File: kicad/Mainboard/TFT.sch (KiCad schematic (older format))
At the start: 2 parts, among them J7 Conn_01x10, Q2 BSS138

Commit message: - Added footprint library - TR-9 - Imported a few footprints - Designed a MicroSD card slot footprint - Assignment footprints to corresponding elements on schematic
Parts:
- J7: footprint (none) -> Connector_FFC-FPC:Hirose_FH12-10S-0.5SH_1x10-1MP_P0.50mm_Horizontal
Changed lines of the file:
@@
 EESchema Schematic File Version 4
-LIBS:Mainboard-cache
 EELAYER 30 0
 EELAYER END
@@
 F 0 "J7" H 6168 3125 50  0000 C CNN
 F 1 "Conn_01x10" H 6168 3216 50  0000 C CNN
-F 2 "" H 6250 3850 50  0001 C CNN
+F 2 "Connector_FFC-FPC:Hirose_FH12-10S-0.5SH_1x10-1MP_P0.50mm_Horizontal" H 6250 3850 50  0001 C CNN
 F 3 "~" H 6250 3850 50  0001 C CNN
 	1    6250 3850

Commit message: Added HMC RF switch Corrected SOIC footprints assignment
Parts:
- Q2: footprint TO_SOT_Packages_SMD:SOT-23 -> Package_TO_SOT_SMD:SOT-23
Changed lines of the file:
@@
 F 0 "Q2" H 4506 3796 50  0000 L CNN
 F 1 "BSS138" H 4506 3705 50  0000 L CNN
-F 2 "TO_SOT_Packages_SMD:SOT-23" H 4500 3675 50  0001 L CIN
+F 2 "Package_TO_SOT_SMD:SOT-23" H 4500 3675 50  0001 L CIN
 F 3 "https://www.fairchildsemi.com/datasheets/BS/BSS138.pdf" H 4300 3750 50  0001 L CNN
 	1    4300 3750

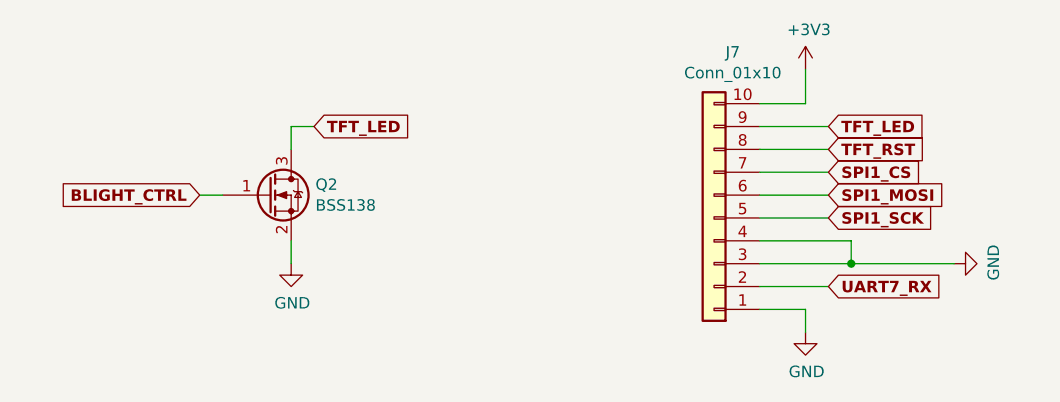
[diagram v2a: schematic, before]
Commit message: Added thermal vias to BGA6589 footprint Corrected USART to UART
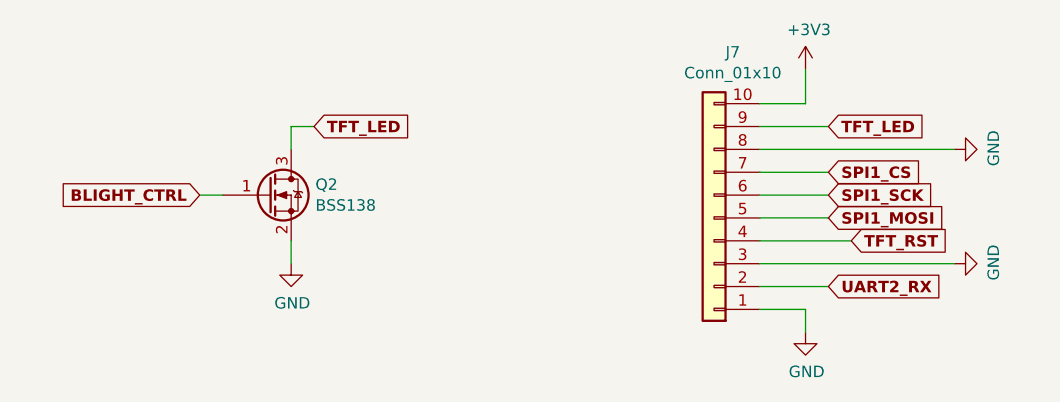
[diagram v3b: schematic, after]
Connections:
- net GND: now also J7.8 (Pin_8); no longer J7.4 (Pin_4)
- net SPI1_MOSI: now also J7.5 (Pin_5); no longer J7.6 (Pin_6)
- net SPI1_SCK: now also J7.6 (Pin_6); no longer J7.5 (Pin_5)
- net TFT_RST: now also J7.4 (Pin_4); no longer J7.8 (Pin_8)
- net UART7_RX renamed UART2_RX
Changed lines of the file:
@@
 Text GLabel 6750 3450 2    50   Input ~ 10
 TFT_LED
-Text GLabel 6750 3550 2    50   Input ~ 10
+Text GLabel 6850 3950 2    50   Input ~ 10
 TFT_RST
 Text GLabel 6750 3650 2    50   Input ~ 10
 SPI1_CS
+Text GLabel 6750 3850 2    50   Input ~ 10
+SPI1_MOSI
 Text GLabel 6750 3750 2    50   Input ~ 10
-SPI1_MOSI
-Text GLabel 6750 3850 2    50   Input ~ 10
 SPI1_SCK
 Wire Wire Line
 	6450 3450 6750 3450
-Wire Wire Line
-	6450 3550 6750 3550
 Wire Wire Line
 	6450 3650 6750 3650
@@
 	6450 4150 6750 4150
 Text GLabel 6750 4150 2    50   Input ~ 10
-UART7_RX
+UART2_RX
 $Comp
 L power:GND #PWR054
@@
 $EndComp
 Wire Wire Line
-	6450 4050 6850 4050
-Wire Wire Line
 	6450 3950 6850 3950
-Wire Wire Line
-	6850 3950 6850 4050
-Connection ~ 6850 4050
-Wire Wire Line
-	6850 4050 7300 4050
 $Comp
 L Mainboard-rescue:Conn_01x10-Connector_Generic J7
@@
 	-1   0    0    1
 $EndComp
+Wire Wire Line
+	6450 4050 7300 4050
+$Comp
+L power:GND #PWR0179
+U 1 1 5E47DF4D
+P 7300 3550
+F 0 "#PWR0179" H 7300 3300 50  0001 C CNN
+F 1 "GND" H 7305 3377 50  0000 C CNN
+F 2 "" H 7300 3550 50  0001 C CNN
+F 3 "" H 7300 3550 50  0001 C CNN
+	1    7300 3550
+	0    -1   -1   0
+$EndComp
+Wire Wire Line
+	6450 3550 7300 3550
 $EndSCHEMATC

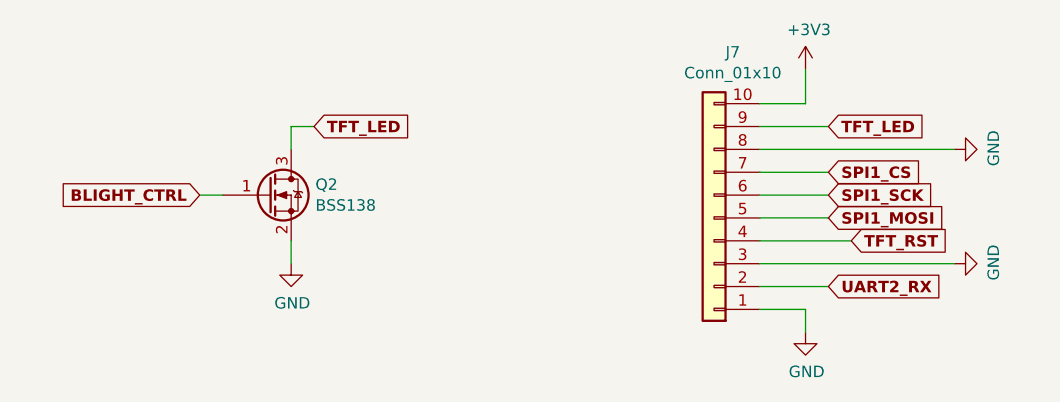
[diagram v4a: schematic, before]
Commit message: PCB - connected microSD card to STM32 & USB frontend path routed added a schottky diode PMEG4005ET.215 footprint changed connector J7 pinout - TFT_RST swapped with UART2_RX! schootky diode added to in series to mini USB connector PDF generated
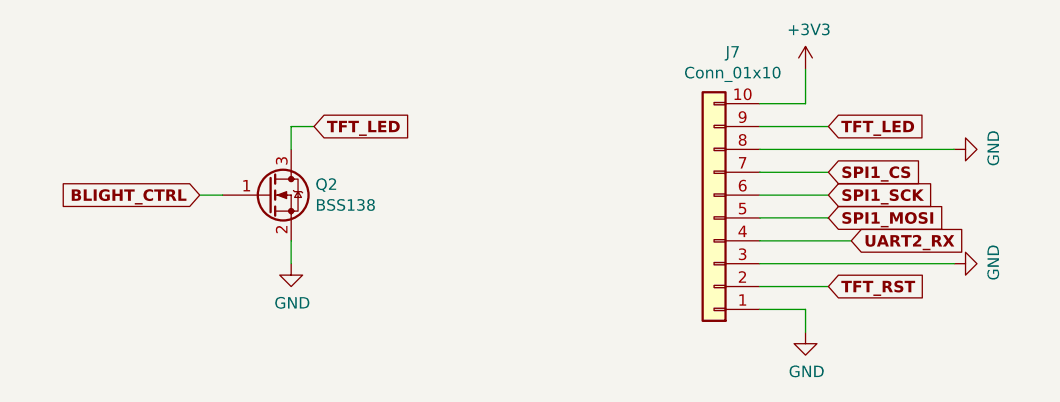
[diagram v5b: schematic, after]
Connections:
- net TFT_RST: now also J7.2 (Pin_2); no longer J7.4 (Pin_4)
- net UART2_RX: now also J7.4 (Pin_4); no longer J7.2 (Pin_2)
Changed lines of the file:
@@
 Text GLabel 6750 3450 2    50   Input ~ 10
 TFT_LED
-Text GLabel 6850 3950 2    50   Input ~ 10
+Text GLabel 6750 4150 2    50   Input ~ 10
 TFT_RST
 Text GLabel 6750 3650 2    50   Input ~ 10
@@
 Wire Wire Line
 	6450 4150 6750 4150
-Text GLabel 6750 4150 2    50   Input ~ 10
+Text GLabel 6850 3950 2    50   Input ~ 10
 UART2_RX
 $Comp

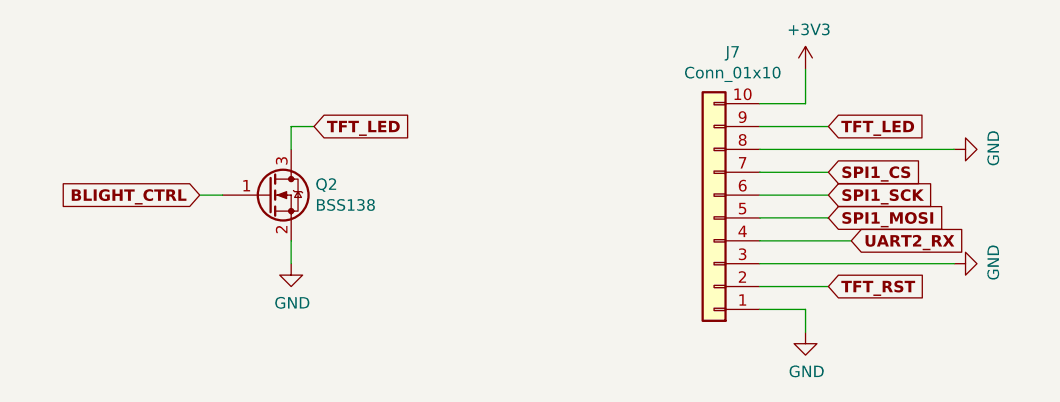
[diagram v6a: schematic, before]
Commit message: Critical J7 header pinout change! New schematic PCB plot
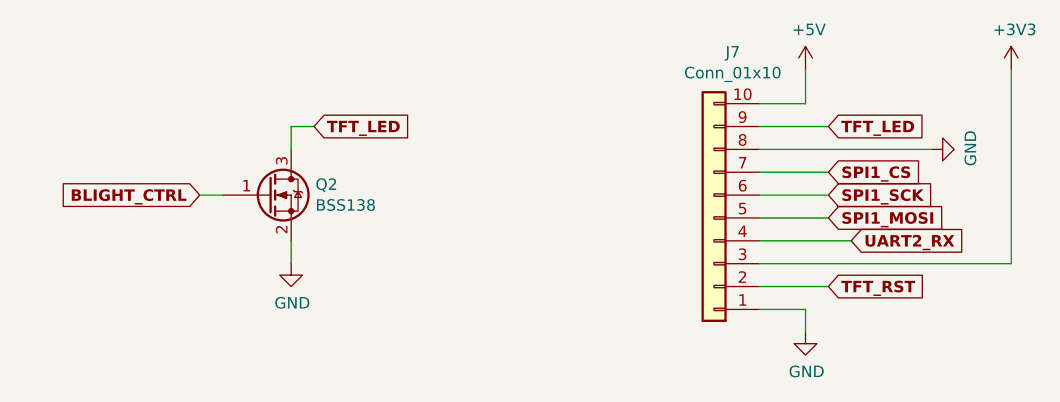
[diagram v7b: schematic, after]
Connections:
- net +3V3: now also J7.3 (Pin_3); no longer J7.10 (Pin_10)
- net GND: no longer J7.3 (Pin_3)
- new net +5V: J7.10 (Pin_10)
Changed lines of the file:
@@
 Wire Wire Line
 	6650 3350 6650 3200
-$Comp
-L power:+3V3 #PWR052
-U 1 1 5DF0DB74
-P 6650 3200
-F 0 "#PWR052" H 6650 3050 50  0001 C CNN
-F 1 "+3V3" H 6665 3373 50  0000 C CNN
-F 2 "" H 6650 3200 50  0001 C CNN
-F 3 "" H 6650 3200 50  0001 C CNN
-	1    6650 3200
-	1    0    0    -1
-$EndComp
 Wire Wire Line
 	6450 4250 6650 4250
@@
 Text GLabel 6850 3950 2    50   Input ~ 10
 UART2_RX
-$Comp
-L power:GND #PWR054
-U 1 1 5E1E62B4
-P 7300 4050
-F 0 "#PWR054" H 7300 3800 50  0001 C CNN
-F 1 "GND" H 7305 3877 50  0000 C CNN
-F 2 "" H 7300 4050 50  0001 C CNN
-F 3 "" H 7300 4050 50  0001 C CNN
-	1    7300 4050
-	0    -1   -1   0
-$EndComp
 Wire Wire Line
 	6450 3950 6850 3950
@@
 	-1   0    0    1
 $EndComp
+$Comp
+L power:+5V #PWR?
+U 1 1 5E4D13A0
+P 6650 3200
+AR Path="/5DEDCA32/5E4D13A0" Ref="#PWR?"  Part="1"
+AR Path="/5DF0AC25/5E4D13A0" Ref="#PWR0179"  Part="1"
+F 0 "#PWR0179" H 6650 3050 50  0001 C CNN
+F 1 "+5V" H 6665 3373 50  0000 C CNN
+F 2 "" H 6650 3200 50  0001 C CNN
+F 3 "" H 6650 3200 50  0001 C CNN
+	1    6650 3200
+	1    0    0    -1
+$EndComp
+$Comp
+L power:+3V3 #PWR?
+U 1 1 5E4D63A8
+P 7550 3200
+AR Path="/5DEDCA32/5E4D63A8" Ref="#PWR?"  Part="1"
+AR Path="/5DF0AC25/5E4D63A8" Ref="#PWR0194"  Part="1"
+F 0 "#PWR0194" H 7550 3050 50  0001 C CNN
+F 1 "+3V3" H 7565 3373 50  0000 C CNN
+F 2 "" H 7550 3200 50  0001 C CNN
+F 3 "" H 7550 3200 50  0001 C CNN
+	1    7550 3200
+	1    0    0    -1
+$EndComp
 Wire Wire Line
-	6450 4050 7300 4050
+	6450 3550 7200 3550
 $Comp
-L power:GND #PWR0179
-U 1 1 5E47DF4D
-P 7300 3550
-F 0 "#PWR0179" H 7300 3300 50  0001 C CNN
-F 1 "GND" H 7305 3377 50  0000 C CNN
-F 2 "" H 7300 3550 50  0001 C CNN
-F 3 "" H 7300 3550 50  0001 C CNN
-	1    7300 3550
+L power:GND #PWR0195
+U 1 1 5E4D8D3B
+P 7200 3550
+F 0 "#PWR0195" H 7200 3300 50  0001 C CNN
+F 1 "GND" H 7205 3377 50  0000 C CNN
+F 2 "" H 7200 3550 50  0001 C CNN
+F 3 "" H 7200 3550 50  0001 C CNN
+	1    7200 3550
 	0    -1   -1   0
 $EndComp
 Wire Wire Line
-	6450 3550 7300 3550
+	7550 3200 7550 4050
+Wire Wire Line
+	6450 4050 7550 4050
 $EndSCHEMATC

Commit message: added some decoupling caps, pull ups/downs
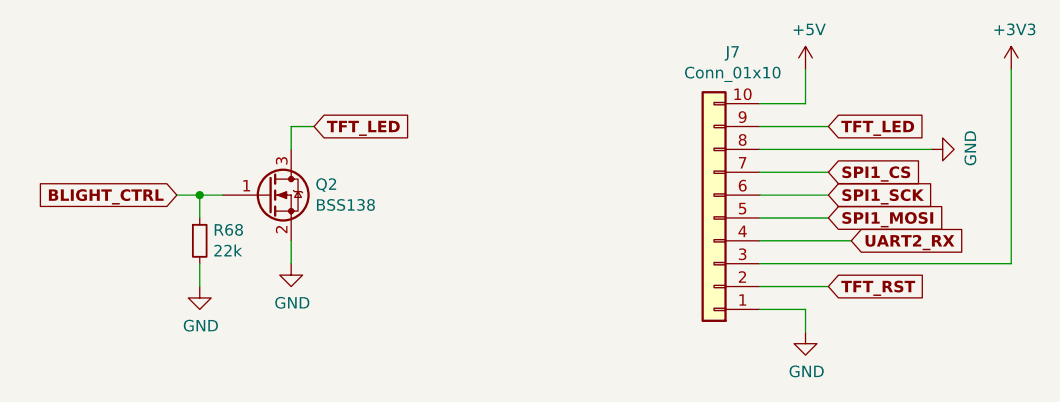
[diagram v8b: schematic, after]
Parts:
- added R68: 22k, Resistor_SMD:R_0603_1608Metric, symbol Mainboard-rescue:R_Small-device
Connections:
- net BLIGHT_CTRL: now also R68.1
- net GND: now also R68.2
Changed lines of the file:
@@
 Wire Wire Line
 	4100 3750 4000 3750
-Text GLabel 4000 3750 0    50   Input ~ 10
+Text GLabel 3900 3750 0    50   Input ~ 10
 BLIGHT_CTRL
 Wire Wire Line
@@
 Wire Wire Line
 	6450 4050 7550 4050
+$Comp
+L Mainboard-rescue:R_Small-device R?
+U 1 1 5E57229A
+P 4000 3950
+AR Path="/5DFC2ACA/5E57229A" Ref="R?"  Part="1"
+AR Path="/5DF0AC25/5E57229A" Ref="R68"  Part="1"
+F 0 "R68" H 4059 3996 50  0000 L CNN
+F 1 "22k" H 4059 3905 50  0000 L CNN
+F 2 "Resistor_SMD:R_0603_1608Metric" H 4000 3950 50  0001 C CNN
+F 3 "~" H 4000 3950 50  0001 C CNN
+	1    4000 3950
+	1    0    0    -1
+$EndComp
+$Comp
+L power:GND #PWR?
+U 1 1 5E5722A6
+P 4000 4150
+AR Path="/5DFC2ACA/5E5722A6" Ref="#PWR?"  Part="1"
+AR Path="/5DF0AC25/5E5722A6" Ref="#PWR0200"  Part="1"
+F 0 "#PWR0200" H 4000 3900 50  0001 C CNN
+F 1 "GND" H 4005 3977 50  0000 C CNN
+F 2 "" H 4000 4150 50  0001 C CNN
+F 3 "" H 4000 4150 50  0001 C CNN
+	1    4000 4150
+	1    0    0    -1
+$EndComp
+Wire Wire Line
+	4000 3750 4000 3850
+Wire Wire Line
+	4000 4050 4000 4150
+Wire Wire Line
+	3900 3750 4000 3750
+Connection ~ 4000 3750
 $EndSCHEMATC
